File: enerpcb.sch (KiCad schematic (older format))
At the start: 22 parts, among them K1 CONN_3, K2 CONN_3, K3 CONN_1, K4 CONN_1, P2 CONN_10, P3 CONN_10, P4 PROGRAM, P5 CONN_10, P6 CONN_10, P7 CONN_10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

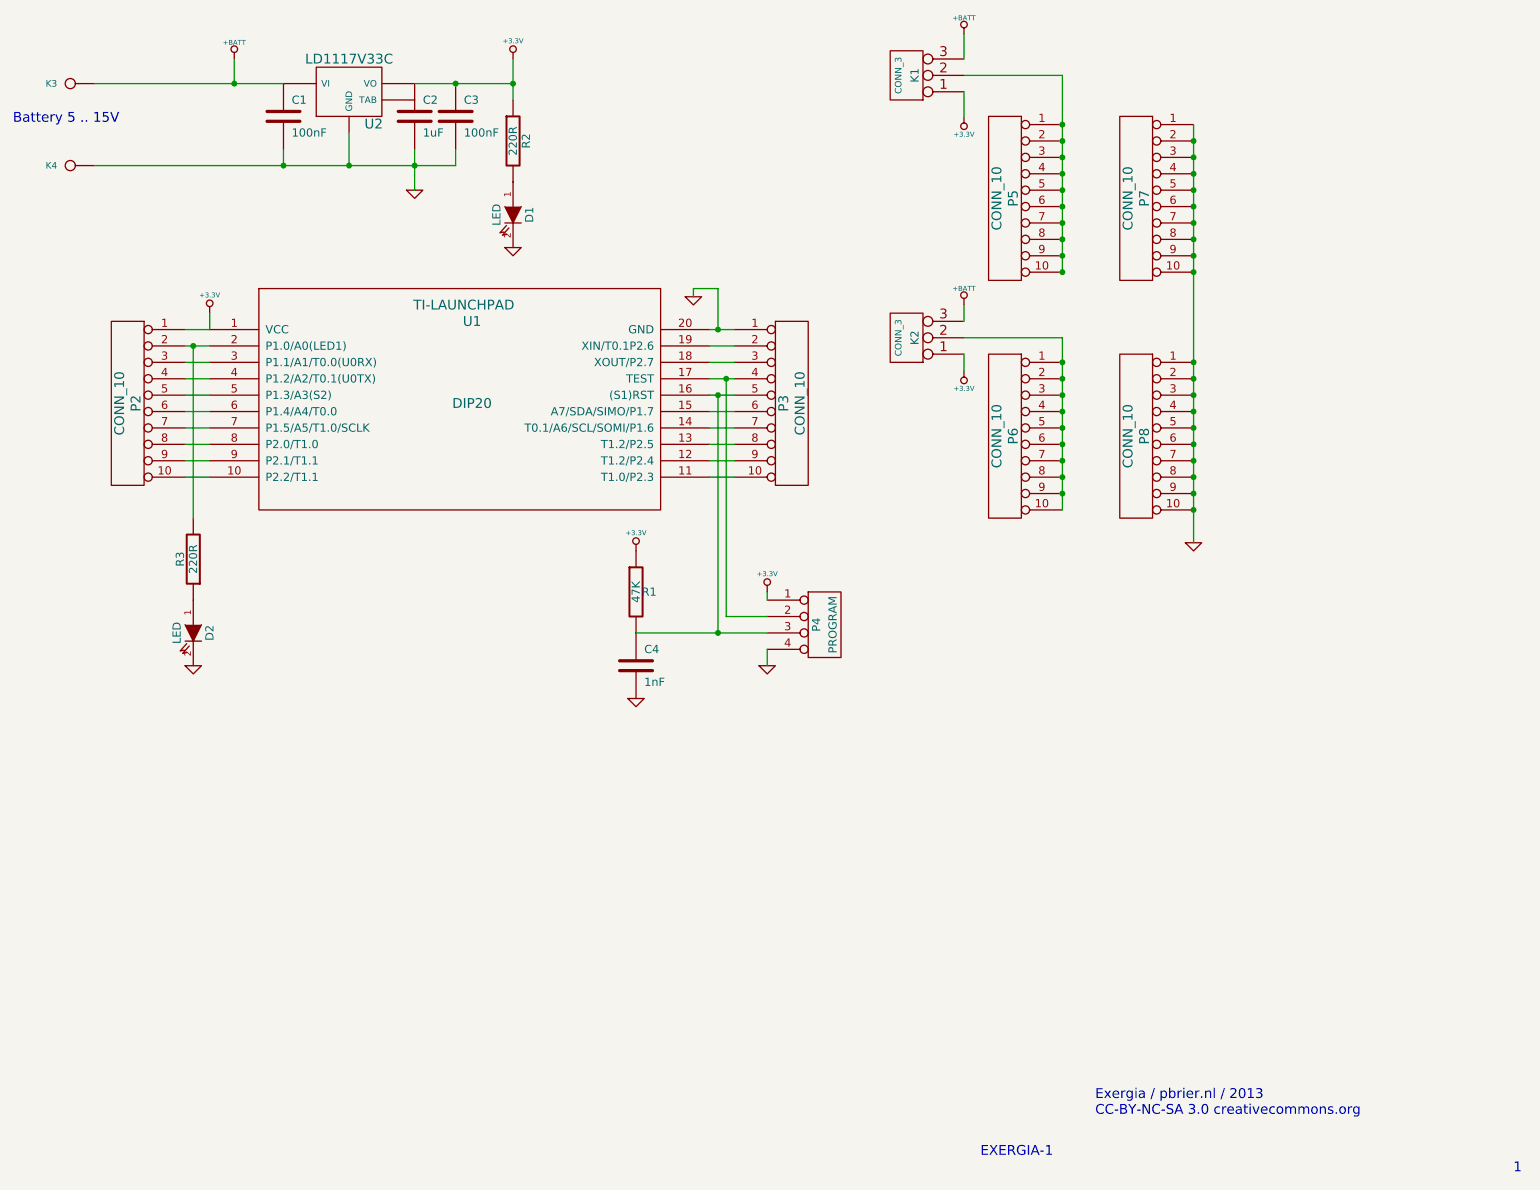
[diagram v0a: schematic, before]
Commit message: Routed the SMB PCB. Seems to be problem with SMD schematic: components gone from lib?
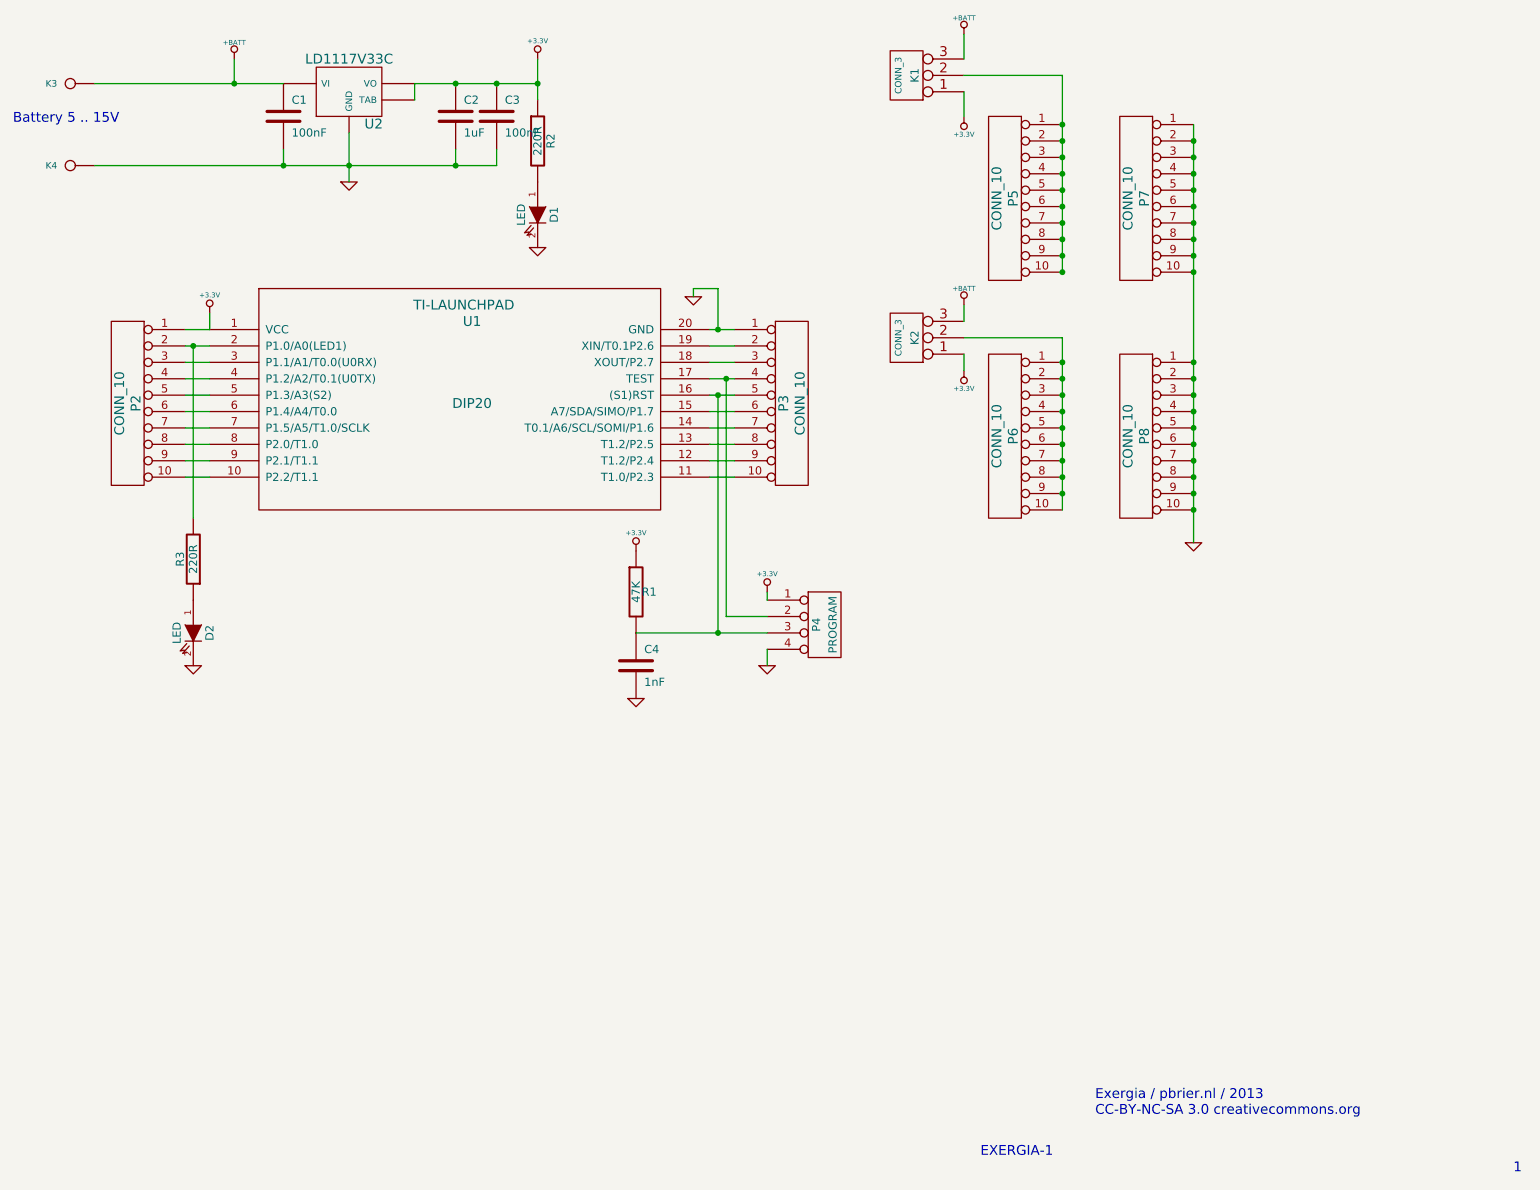
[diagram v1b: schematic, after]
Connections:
- net +3.3V: now also U2.4 (TAB)
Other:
- moved on the sheet: C2, C3, D1, R2
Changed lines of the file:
@@
-EESchema Schematic File Version 2  date 1/1/2013 6:47:40 PM
+EESchema Schematic File Version 2  date 1/5/2013 3:48:10 PM
+LIBS:ti-launchpad
 LIBS:power
 LIBS:device
@@
 LIBS:contrib
 LIBS:valves
-LIBS:ti-launchpad
 LIBS:enerpcb-cache
 EELAYER 25  0
@@
 Sheet 1 1
 Title ""
-Date "1 jan 2013"
+Date "5 jan 2013"
 Rev ""
 Comp ""
@@
 Comment4 ""
 $EndDescr
+Wire Wire Line
+	2050 1500 4500 1500
+Wire Wire Line
+	4500 1500 4500 1400
+Connection ~ 4500 1000
+Wire Wire Line
+	4750 1000 4000 1000
+Wire Wire Line
+	5800 2700 5950 2700
+Connection ~ 5900 2800
+Wire Wire Line
+	5900 2800 5900 4250
+Wire Wire Line
+	5950 3400 5800 3400
+Wire Wire Line
+	5950 3200 5800 3200
+Wire Wire Line
+	5950 3000 5800 3000
+Wire Wire Line
+	5950 2800 5800 2800
+Connection ~ 2650 2600
+Wire Wire Line
+	2650 2600 2650 3650
+Wire Wire Line
+	2600 3300 2750 3300
+Wire Wire Line
+	2600 3100 2750 3100
+Wire Wire Line
+	2600 2900 2750 2900
+Wire Wire Line
+	2600 2700 2750 2700
+Wire Wire Line
+	2600 2500 2750 2500
+Wire Wire Line
+	6150 4350 5350 4350
+Wire Wire Line
+	6150 4450 6150 4550
+Connection ~ 4750 1000
+Wire Wire Line
+	4750 850  4750 1100
+Wire Wire Line
+	2050 1000 3200 1000
+Connection ~ 3200 1500
+Wire Wire Line
+	3200 1500 3200 1400
+Wire Wire Line
+	8750 1250 8750 3800
+Wire Wire Line
+	7950 3600 7950 2550
+Wire Wire Line
+	7950 2550 7350 2550
+Wire Wire Line
+	7350 2350 7350 2450
+Connection ~ 8750 3600
+Connection ~ 8750 3400
+Connection ~ 8750 3200
+Connection ~ 8750 3100
+Connection ~ 8750 2900
+Connection ~ 8750 2050
+Connection ~ 8750 1850
+Connection ~ 8750 1750
+Connection ~ 8750 1550
+Connection ~ 8750 1350
+Connection ~ 7950 3500
+Connection ~ 7950 3300
+Connection ~ 7950 3000
+Connection ~ 7950 2800
+Connection ~ 7950 2150
+Connection ~ 7950 1950
+Connection ~ 7950 1750
+Connection ~ 7950 1550
+Connection ~ 7950 1350
+Wire Wire Line
+	7350 950  7950 950
+Wire Wire Line
+	7350 700  7350 850
+Wire Wire Line
+	5700 2300 5700 2250
+Wire Wire Line
+	2750 2500 2750 2400
+Wire Wire Line
+	2900 850  2900 1000
+Connection ~ 2900 1000
+Wire Wire Line
+	7350 1200 7350 1050
+Connection ~ 7950 1250
+Connection ~ 7950 1450
+Connection ~ 7950 1650
+Connection ~ 7950 1850
+Connection ~ 7950 2050
+Connection ~ 7950 2700
+Connection ~ 7950 2900
+Connection ~ 7950 3200
+Connection ~ 7950 3100
+Connection ~ 7950 3400
+Connection ~ 8750 1450
+Connection ~ 8750 1650
+Connection ~ 8750 1950
+Connection ~ 8750 2150
+Connection ~ 8750 2800
+Connection ~ 8750 2700
+Connection ~ 8750 3000
+Connection ~ 8750 3300
+Connection ~ 8750 3500
+Wire Wire Line
+	7950 950  7950 2150
+Wire Wire Line
+	7350 2650 7350 2750
+Connection ~ 3600 1500
+Wire Wire Line
+	6150 4150 6150 4100
+Wire Wire Line
+	2600 2600 2750 2600
+Wire Wire Line
+	2600 2800 2750 2800
+Wire Wire Line
+	2600 3000 2750 3000
+Wire Wire Line
+	2600 3200 2750 3200
+Wire Wire Line
+	2600 3400 2750 3400
+Wire Wire Line
+	5800 2500 5950 2500
+Wire Wire Line
+	5950 2900 5800 2900
+Wire Wire Line
+	5950 3100 5800 3100
+Wire Wire Line
+	5950 3300 5800 3300
+Wire Wire Line
+	5700 2250 5850 2250
+Wire Wire Line
+	5850 2250 5850 2500
+Connection ~ 5850 2500
+Wire Wire Line
+	5900 4250 6150 4250
+Wire Wire Line
+	5850 2900 5850 4350
+Connection ~ 5850 4350
+Connection ~ 5850 2900
+Wire Wire Line
+	5950 2600 5800 2600
+Wire Wire Line
+	4000 1000 4000 1100
+Connection ~ 4250 1000
+Wire Wire Line
+	4250 1400 4250 1500
+Connection ~ 4250 1500
+Wire Wire Line
+	3600 1600 3600 1300
 Text Notes 1550 1250 0    60   ~ 0
 Battery 5 .. 15V
@@
 Text Notes 7450 7550 0    60   ~ 0
 EXERGIA-1
-Connection ~ 5850 2900
-Connection ~ 5850 4350
-Wire Wire Line
-	5850 2900 5850 4350
-Wire Wire Line
-	6150 4250 5900 4250
-Connection ~ 5850 2500
-Wire Wire Line
-	5850 2500 5850 2250
-Wire Wire Line
-	5850 2250 5700 2250
-Wire Wire Line
-	5950 3300 5800 3300
-Wire Wire Line
-	5950 3100 5800 3100
-Wire Wire Line
-	5950 2900 5800 2900
-Wire Wire Line
-	5950 2700 5800 2700
-Wire Wire Line
-	5800 2500 5950 2500
-Wire Wire Line
-	2600 3400 2750 3400
-Wire Wire Line
-	2600 3200 2750 3200
-Wire Wire Line
-	2600 3000 2750 3000
-Wire Wire Line
-	2600 2800 2750 2800
-Wire Wire Line
-	2600 2600 2750 2600
-Wire Wire Line
-	6150 4150 6150 4100
-Connection ~ 4250 1000
-Wire Wire Line
-	4250 1400 4250 1500
-Wire Wire Line
-	4250 1500 2050 1500
-Connection ~ 3600 1500
-Wire Wire Line
-	3600 1500 3600 1300
-Wire Wire Line
-	7350 2650 7350 2750
-Wire Wire Line
-	7950 2150 7950 950
-Connection ~ 8750 3500
-Connection ~ 8750 3300
-Connection ~ 8750 3000
-Connection ~ 8750 2700
-Connection ~ 8750 2800
-Connection ~ 8750 2150
-Connection ~ 8750 1950
-Connection ~ 8750 1650
-Connection ~ 8750 1450
-Connection ~ 7950 3400
-Connection ~ 7950 3100
-Connection ~ 7950 3200
-Connection ~ 7950 2900
-Connection ~ 7950 2700
-Connection ~ 7950 2050
-Connection ~ 7950 1850
-Connection ~ 7950 1650
-Connection ~ 7950 1450
-Connection ~ 7950 1250
-Wire Wire Line
-	7350 1200 7350 1050
-Connection ~ 2900 1000
-Wire Wire Line
-	2900 850  2900 1000
-Wire Wire Line
-	2750 2400 2750 2500
-Wire Wire Line
-	5700 2250 5700 2300
-Wire Wire Line
-	7350 700  7350 850
-Wire Wire Line
-	7950 950  7350 950
-Connection ~ 7950 1350
-Connection ~ 7950 1550
-Connection ~ 7950 1750
-Connection ~ 7950 1950
-Connection ~ 7950 2150
-Connection ~ 7950 2800
-Connection ~ 7950 3000
-Connection ~ 7950 3300
-Connection ~ 7950 3500
-Connection ~ 8750 1350
-Connection ~ 8750 1550
-Connection ~ 8750 1750
-Connection ~ 8750 1850
-Connection ~ 8750 2050
-Connection ~ 8750 2900
-Connection ~ 8750 3100
-Connection ~ 8750 3200
-Connection ~ 8750 3400
-Connection ~ 8750 3600
-Wire Wire Line
-	7350 2350 7350 2450
-Wire Wire Line
-	7350 2550 7950 2550
-Wire Wire Line
-	7950 2550 7950 3600
-Wire Wire Line
-	8750 1250 8750 3800
-Wire Wire Line
-	3200 1500 3200 1400
-Connection ~ 3200 1500
-Connection ~ 4000 1500
-Wire Wire Line
-	4000 1650 4000 1400
-Wire Wire Line
-	2050 1000 3200 1000
-Wire Wire Line
-	4600 1000 4000 1000
-Wire Wire Line
-	4600 850  4600 1100
-Connection ~ 4600 1000
-Wire Wire Line
-	6150 4450 6150 4550
-Wire Wire Line
-	6150 4350 5350 4350
-Wire Wire Line
-	2750 2500 2600 2500
-Wire Wire Line
-	2600 2700 2750 2700
-Wire Wire Line
-	2600 2900 2750 2900
-Wire Wire Line
-	2600 3100 2750 3100
-Wire Wire Line
-	2600 3300 2750 3300
-Wire Wire Line
-	2650 2600 2650 3650
-Connection ~ 2650 2600
-Wire Wire Line
-	5950 2600 5800 2600
-Wire Wire Line
-	5950 2800 5800 2800
-Wire Wire Line
-	5950 3000 5800 3000
-Wire Wire Line
-	5950 3200 5800 3200
-Wire Wire Line
-	5950 3400 5800 3400
-Wire Wire Line
-	5900 4250 5900 2800
-Connection ~ 5900 2800
 $Comp
 L +3.3V #PWR01
@@
 L C C3
 U 1 1 50E2C4B7
-P 4250 1200
-F 0 "C3" H 4300 1300 50  0000 L CNN
-F 1 "100nF" H 4300 1100 50  0000 L CNN
-	1    4250 1200
+P 4500 1200
+F 0 "C3" H 4550 1300 50  0000 L CNN
+F 1 "100nF" H 4550 1100 50  0000 L CNN
+	1    4500 1200
 	1    0    0    -1
 $EndComp
@@
 L GND #PWR04
 U 1 1 50E1B581
-P 4000 1650
-F 0 "#PWR04" H 4000 1650 30  0001 C CNN
-F 1 "GND" H 4000 1580 30  0001 C CNN
-	1    4000 1650
+P 3600 1600
+F 0 "#PWR04" H 3600 1600 30  0001 C CNN
+F 1 "GND" H 3600 1530 30  0001 C CNN
+	1    3600 1600
 	1    0    0    -1
 $EndComp
@@
 L R R2
 U 1 1 50E1AB7A
-P 4600 1350
-F 0 "R2" V 4680 1350 50  0000 C CNN
-F 1 "220R" V 4600 1350 50  0000 C CNN
-	1    4600 1350
+P 4750 1350
+F 0 "R2" V 4830 1350 50  0000 C CNN
+F 1 "220R" V 4750 1350 50  0000 C CNN
+	1    4750 1350
 	1    0    0    -1
 $EndComp
@@
 L LED D1
 U 1 1 50E1AB6E
-P 4600 1800
-F 0 "D1" H 4600 1900 50  0000 C CNN
-F 1 "LED" H 4600 1700 50  0000 C CNN
-	1    4600 1800
+P 4750 1800
+F 0 "D1" H 4750 1900 50  0000 C CNN
+F 1 "LED" H 4750 1700 50  0000 C CNN
+	1    4750 1800
 	0    1    1    0
 $EndComp
@@
 L GND #PWR011
 U 1 1 50E196DA
-P 4600 2000
-F 0 "#PWR011" H 4600 2000 30  0001 C CNN
-F 1 "GND" H 4600 1930 30  0001 C CNN
-	1    4600 2000
+P 4750 2000
+F 0 "#PWR011" H 4750 2000 30  0001 C CNN
+F 1 "GND" H 4750 1930 30  0001 C CNN
+	1    4750 2000
 	1    0    0    -1
 $EndComp
@@
 L +3.3V #PWR012
 U 1 1 50E196C9
-P 4600 850
-F 0 "#PWR012" H 4600 810 30  0001 C CNN
-F 1 "+3.3V" H 4600 960 30  0000 C CNN
-	1    4600 850
+P 4750 850
+F 0 "#PWR012" H 4750 810 30  0001 C CNN
+F 1 "+3.3V" H 4750 960 30  0000 C CNN
+	1    4750 850
 	1    0    0    -1
 $EndComp
@@
 L C C2
 U 1 1 50E1969F
-P 4000 1200
-F 0 "C2" H 4050 1300 50  0000 L CNN
-F 1 "1uF" H 4050 1100 50  0000 L CNN
-	1    4000 1200
-	1    0    0    -1
-$EndComp
+P 4250 1200
+F 0 "C2" H 4300 1300 50  0000 L CNN
+F 1 "1uF" H 4300 1100 50  0000 L CNN
+	1    4250 1200
+	1    0    0    -1
+$EndComp
